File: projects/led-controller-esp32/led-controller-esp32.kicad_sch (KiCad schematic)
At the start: 9 parts, among them J1 Conn_01x02, J2 LED PIGTAIL, U1 XIAO ESP32C3, U2 DC Buck 5V

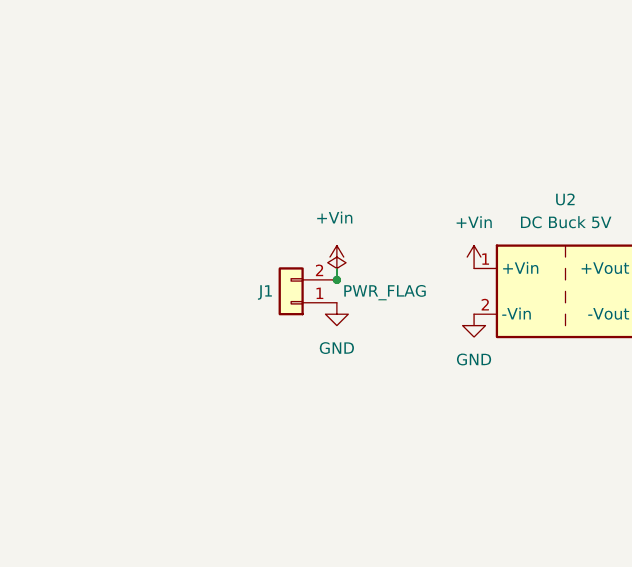
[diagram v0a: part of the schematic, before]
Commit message: use standard 2 screw terminal and other tidy ups
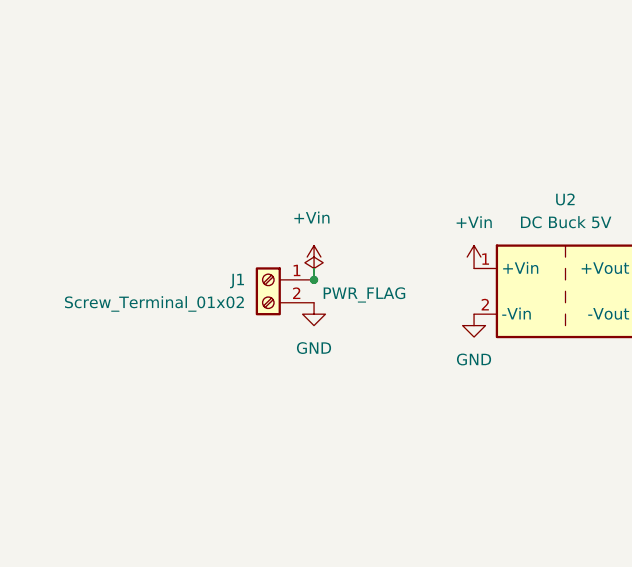
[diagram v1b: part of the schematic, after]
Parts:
- removed J1: Conn_01x02, Connector_PinHeader_2.54mm:PinHeader_1x02_P2.54mm_Vertical, symbol Connector_Generic:Conn_01x02
- added J1: Screw_Terminal_01x02, TerminalBlock_Phoenix:TerminalBlock_Phoenix_MKDS-1,5-2-5.08_1x02_P5.08mm_Horizontal, symbol Connector:Screw_Terminal_01x02
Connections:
- net +Vin: now also J1.1 (Pin_1)
- net GND: now also J1.2 (Pin_2)
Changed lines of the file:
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@@
-	)
-	(junction
-		(at 43.18 76.2)
-		(diameter 0)
-		(color 0 0 0 0)
 	)
 	(junction
@@
 		(color 0 0 0 0)
 	)
+	(junction
+		(at 40.64 76.2)
+		(diameter 0)
+		(color 0 0 0 0)
+	)
 	(no_connect
 		(at 138.43 120.65)
@@
 	(wire
 		(pts
+			(xy 40.64 74.93) (xy 40.64 76.2)
+		)
+		(stroke
+			(width 0)
+			(type default)
+		)
+	)
+	(wire
+		(pts
 			(xy 127 66.04) (xy 137.16 66.04)
 		)
@@
 		(pts
 			(xy 137.16 69.85) (xy 137.16 68.58)
-		)
-		(stroke
-			(width 0)
-			(type default)
-		)
-	)
-	(wire
-		(pts
-			(xy 43.18 74.93) (xy 43.18 76.2)
 		)
 		(stroke
@@
 	(symbol
 		(lib_id "power:PWR_FLAG")
-		(at 43.18 76.2 0)
+		(at 40.64 76.2 0)
 		(unit 1)
 		(exclude_from_sim no)
@@
 		(dnp no)
 		(property "Reference" "#FLG01"
-			(at 43.18 74.295 0)
+			(at 40.64 74.295 0)
 			(effects
 				(font
@@
 		)
 		(property "Value" "PWR_FLAG"
-			(at 48.514 77.47 0)
+			(at 46.228 77.724 0)
 			(effects
 				(font
@@
 		)
 		(property "Footprint" ""
-			(at 43.18 76.2 0)
+			(at 40.64 76.2 0)
 			(effects
 				(font
@@
 		)
 		(property "Datasheet" "~"
-			(at 43.18 76.2 0)
+			(at 40.64 76.2 0)
 			(effects
 				(font
@@
 		)
 		(property "Description" "Special symbol for telling ERC where power comes from"
-			(at 43.18 76.2 0)
+			(at 40.64 76.2 0)
 			(effects
 				(font
@@
 				(path "/684d0112-cd7c-404f-9d38-ab09c0c867b6"
 					(reference "#FLG01")
+					(unit 1)
+				)
+			)
+		)
+	)
+	(symbol
+		(lib_id "Connector:Screw_Terminal_01x02")
+		(at 35.56 76.2 0)
+		(mirror y)
+		(unit 1)
+		(exclude_from_sim no)
+		(in_bom yes)
+		(on_board yes)
+		(dnp no)
+		(property "Reference" "J1"
+			(at 33.02 76.1999 0)
+			(effects
+				(font
+					(size 1.27 1.27)
+				)
+				(justify left)
+			)
+		)
+		(property "Value" "Screw_Terminal_01x02"
+			(at 33.02 78.7399 0)
+			(effects
+				(font
+					(size 1.27 1.27)
+				)
+				(justify left)
+			)
+		)
+		(property "Footprint" "TerminalBlock_Phoenix:TerminalBlock_Phoenix_MKDS-1,5-2-5.08_1x02_P5.08mm_Horizontal"
+			(at 35.56 76.2 0)
+			(effects
+				(font
+					(size 1.27 1.27)
+				)
+				(hide yes)
+			)
+		)
+		(property "Datasheet" "~"
+			(at 35.56 76.2 0)
+			(effects
+				(font
+					(size 1.27 1.27)
+				)
+				(hide yes)
+			)
+		)
+		(property "Description" "Generic screw terminal, single row, 01x02, script generated (kicad-library-utils/schlib/autogen/connector/)"
+			(at 35.56 76.2 0)
+			(effects
+				(font
+					(size 1.27 1.27)
+				)
+				(hide yes)
+			)
+		)
+		(pin "1"
+		)
+		(pin "2"
+		)
+		(instances
+			(project ""
+				(path "/684d0112-cd7c-404f-9d38-ab09c0c867b6"
+					(reference "J1")
 					(unit 1)
 				)
@@
 	(symbol
 		(lib_id "power:+5V")
-		(at 43.18 74.93 0)
+		(at 40.64 74.93 0)
 		(unit 1)
 		(exclude_from_sim no)
@@
 		(dnp no)
 		(property "Reference" "#PWR014"
-			(at 43.18 78.74 0)
+			(at 40.64 78.74 0)
 			(effects
 				(font
@@
 		)
 		(property "Value" "+Vin"
-			(at 42.926 69.342 0)
+			(at 40.386 69.342 0)
 			(effects
 				(font
@@
 		)
 		(property "Footprint" ""
-			(at 43.18 74.93 0)
+			(at 40.64 74.93 0)
 			(effects
 				(font
@@
 		)
 		(property "Datasheet" ""
-			(at 43.18 74.93 0)
+			(at 40.64 74.93 0)
 			(effects
 				(font
@@
 		)
 		(property "Description" "Power symbol creates a global label with name \"+5V\""
-			(at 43.18 74.93 0)
+			(at 40.64 74.93 0)
 			(effects
 				(font
@@
 	)
 	(symbol
-		(lib_id "Connector_Generic:Conn_01x02")
-		(at 38.1 78.74 180)
-		(unit 1)
-		(exclude_from_sim no)
-		(in_bom yes)
-		(on_board yes)
-		(dnp no)
-		(property "Reference" "J1"
-			(at 35.306 77.47 0)
-			(effects
-				(font
-					(size 1.27 1.27)
-				)
-			)
-		)
-		(property "Value" "Conn_01x02"
-			(at 35.052 82.296 0)
-			(effects
-				(font
-					(size 1.27 1.27)
-				)
-				(hide yes)
-			)
-		)
-		(property "Footprint" "Connector_PinHeader_2.54mm:PinHeader_1x02_P2.54mm_Vertical"
-			(at 38.1 78.74 0)
-			(effects
-				(font
-					(size 1.27 1.27)
-				)
-				(hide yes)
-			)
-		)
-		(property "Datasheet" "~"
-			(at 38.1 78.74 0)
-			(effects
-				(font
-					(size 1.27 1.27)
-				)
-				(hide yes)
-			)
-		)
-		(property "Description" "Generic connector, single row, 01x02, script generated (kicad-library-utils/schlib/autogen/connector/)"
-			(at 38.1 78.74 0)
-			(effects
-				(font
-					(size 1.27 1.27)
-				)
-				(hide yes)
-			)
-		)
-		(pin "1"
-		)
-		(pin "2"
-		)
-		(instances
-			(project ""
-				(path "/684d0112-cd7c-404f-9d38-ab09c0c867b6"
-					(reference "J1")
-					(unit 1)
-				)
-			)
-		)
-	)
-	(symbol
 		(lib_id "power:GND")
-		(at 43.18 78.74 0)
+		(at 40.64 78.74 0)
 		(unit 1)
 		(exclude_from_sim no)
@@
 		(fields_autoplaced yes)
 		(property "Reference" "#PWR011"
-			(at 43.18 85.09 0)
+			(at 40.64 85.09 0)
 			(effects
 				(font
@@
 		)
 		(property "Value" "GND"
-			(at 43.18 83.82 0)
+			(at 40.64 83.82 0)
 			(effects
 				(font
@@
 		)
 		(property "Footprint" ""
-			(at 43.18 78.74 0)
+			(at 40.64 78.74 0)
 			(effects
 				(font
@@
 		)
 		(property "Datasheet" ""
-			(at 43.18 78.74 0)
+			(at 40.64 78.74 0)
 			(effects
 				(font
@@
 		)
 		(property "Description" "Power symbol creates a global label with name \"GND\" , ground"
-			(at 43.18 78.74 0)
-			(effects
-				(font
+			(at 40.64 78.74 0)
+			(effects
+				(font

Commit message: label terminal blocks and other cleanups
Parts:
- J2: footprint Connector_PinHeader_2.54mm:PinHeader_1x03_P2.54mm_Vertical -> TerminalBlock_Phoenix:TerminalBlock_Phoenix_MKDS-1,5-3-5.08_1x03_P5.08mm_Horizontal; symbol Connector_Generic:Conn_01x03 -> Connector:Screw_Terminal_01x03
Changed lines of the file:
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@@
 	)
 	(symbol
-		(lib_id "Connector_Generic:Conn_01x03")
+		(lib_id "Connector:Screw_Terminal_01x03")
 		(at 142.24 66.04 0)
 		(unit 1)
@@
 			)
 		)
-		(property "Footprint" "Connector_PinHeader_2.54mm:PinHeader_1x03_P2.54mm_Vertical"
+		(property "Footprint" "TerminalBlock_Phoenix:TerminalBlock_Phoenix_MKDS-1,5-3-5.08_1x03_P5.08mm_Horizontal"
 			(at 142.24 66.04 0)
 			(effects
@@
 			)
 		)
-		(property "Description" "Generic connector, single row, 01x03, script generated (kicad-library-utils/schlib/autogen/connector/)"
+		(property "Description" "Generic screw terminal, single row, 01x03, script generated (kicad-library-utils/schlib/autogen/connector/)"
 			(at 142.24 66.04 0)
 			(effects
